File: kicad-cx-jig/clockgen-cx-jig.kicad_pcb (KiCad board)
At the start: 2 copper layers, 20.2 x 12 mm, 10 parts, among them J1 Conn_Coaxial, J2 Conn_01x01_Pin, J3 Conn_01x01_Pin, J4 Conn_01x01_Pin, J5 Conn_01x01_Pin

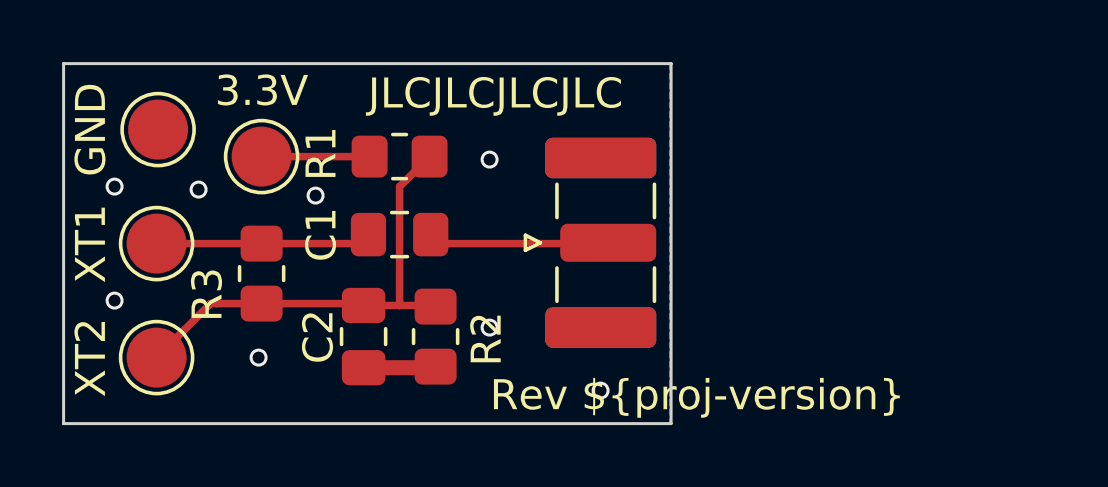
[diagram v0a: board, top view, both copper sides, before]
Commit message: Add board reference variable to project configuration
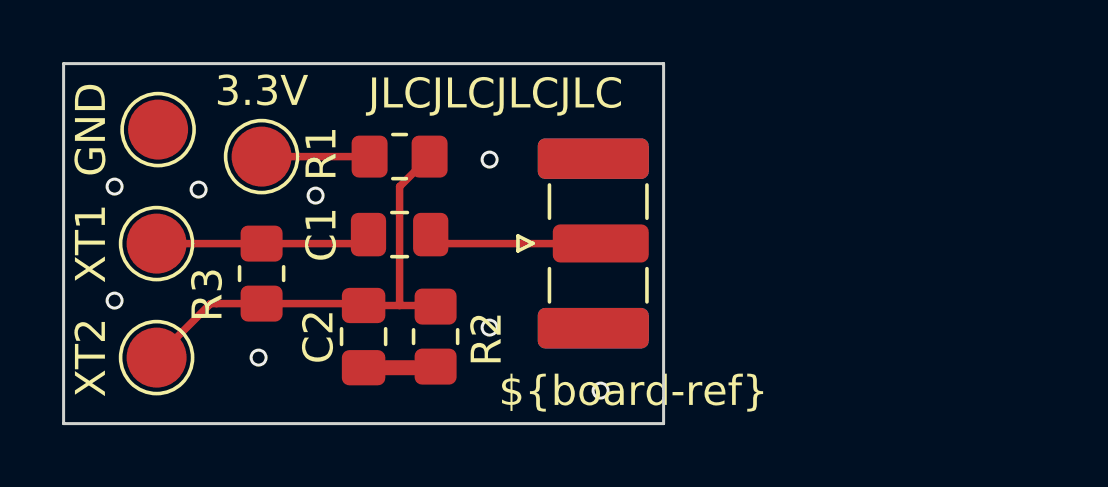
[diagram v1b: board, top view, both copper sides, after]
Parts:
- added ${board-ref}**: Board, PCM_kikit:Board, F.Cu at (125.0, 75.0)
- moved J1 0.25 mm to (142.9, 81.0)
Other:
- board size 20.2 x 12 mm -> 20 x 12 mm
- board text added: "${board-ref}"
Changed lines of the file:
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@@
 		(capping no)
 		(filling no)
-		(zone_defaults)
 		(pcbplotparams
 			(layerselection 0x00000000_00000000_55555555_5755f5ff)
@@
 		)
 	)
+	(property "board-ref" "CX_JIG")
 	(property "proj-author" "Reece Dodge")
 	(property "proj-company" "GDH Technologies LLC")
@@
 			(at 0 2.05 0)
 			(layer "F.Fab")
+			(hide yes)
 			(effects
 				(font
@@
 		(embedded_fonts no)
 	)
+	(footprint "PCM_kikit:Board"
+		(layer "F.Cu")
+		(at 125 75)
+		(descr "Mark board for extraction")
+		(property "Reference" "${board-ref}**"
+			(at -4.5 -5 0)
+			(layer "Dwgs.User")
+			(effects
+				(font
+					(size 1 1)
+					(thickness 0.15)
+				)
+				(justify left)
+			)
+		)
+		(property "Value" "Board"
+			(at -7.25 -5 0)
+			(layer "Dwgs.User")
+			(effects
+				(font
+					(size 1 1)
+					(thickness 0.15)
+				)
+			)
+		)
+		(property "Datasheet" ""
+			(at 0 0 0)
+			(layer "F.Fab")
+			(hide yes)
+			(effects
+				(font
+					(size 1.27 1.27)
+				)
+			)
+		)
+		(property "Description" ""
+			(at 0 0 0)
+			(layer "F.Fab")
+			(hide yes)
+			(effects
+				(font
+					(size 1.27 1.27)
+				)
+			)
+		)
+		(attr board_only exclude_from_pos_files exclude_from_bom allow_missing_courtyard)
+		(duplicate_pad_numbers_are_jumpers no)
+		(fp_line
+			(start -1.25 -4)
+			(end -9.25 -4)
+			(stroke
+				(width 0.2)
+				(type solid)
+			)
+			(layer "Dwgs.User")
+		)
+		(fp_line
+			(start 0 0)
+			(end -1.25 -4)
+			(stroke
+				(width 0.2)
+				(type solid)
+			)
+			(layer "Dwgs.User")
+		)
+		(fp_line
+			(start 0 0)
+			(end -1 -0.5)
+			(stroke
+				(width 0.2)
+				(type solid)
+			)
+			(layer "Dwgs.User")
+		)
+		(fp_line
+			(start 0 0)
+			(end 0.5 -1)
+			(stroke
+				(width 0.2)
+				(type solid)
+			)
+			(layer "Dwgs.User")
+		)
+		(embedded_fonts no)
+	)
 	(footprint "Resistor_SMD:R_0805_2012Metric_Pad1.20x1.40mm_HandSolder"
 		(layer "F.Cu")
@@
 	(footprint "Connector_Coaxial:SMA_Samtec_SMA-J-P-H-ST-EM1_EdgeMount"
 		(layer "F.Cu")
-		(at 143.155182 80.972275)
+		(at 142.905182 80.99455)
 		(descr "Connector SMA, 0Hz to 20GHz, 50Ohm, Edge Mount (http://suddendocs.samtec.com/prints/sma-j-p-x-st-em1-mkt.pdf)")
 		(tags "SMA Straight Samtec Edge Mount")
@@
 			(at 0 7.62 0)
 			(layer "F.Fab")
+			(hide yes)
 			(effects
 				(font
@@
 					(size 0.5 0.5)
 					(thickness 0.1)
-				)
-			)
-		)
-		(fp_text user "Board Thickness: 1.57mm"
-			(at 0 5.079999 0)
-			(layer "Cmts.User")
-			(effects
-				(font
-					(size 1 1)
-					(thickness 0.15)
 				)
 			)
@@
 			(at 0 2.05 0)
 			(layer "F.Fab")
+			(hide yes)
 			(effects
 				(font
@@
 			(layer "F.CrtYd")
 		)
-		(fp_text user "${REFERENCE}"
-			(at 0 -2 0)
-			(layer "F.Fab")
-			(effects
-				(font
-					(size 1 1)
-					(thickness 0.15)
-				)
-			)
-		)
 		(pad "1" smd circle
 			(at 0 0)
@@
 			(at 0 2.05 0)
 			(layer "F.Fab")
+			(hide yes)
 			(effects
 				(font
@@
 	(gr_rect
 		(start 125 75)
-		(end 145.25 87)
+		(end 145 87)
+		(radius 1)
 		(stroke
 			(width 0.1)
-			(type default)
+			(type solid)
 		)
 		(fill no)
 		(layer "Edge.Cuts")
 	)
-	(gr_text "Rev ${REVISION}"
-		(at 139.210441 86.641979 0)
+	(gr_text "${board-ref}"
+		(at 139.5 86.5 0)
 		(layer "F.SilkS")
 		(effects
@@
 			)
 			(justify bottom)
+		)
+	)
+	(gr_text "Rev ${REVISION}"
+		(at 144.710441 86.641979 -0)
+		(layer "B.SilkS")
+		(effects
+			(font
+				(size 1 1)
+				(thickness 0.15)
+			)
+			(justify left bottom mirror)
 		)
 	)
@@
 		)
 		(knockout no)
+	)
+	(point
+		(at 125 75)
+		(size 1)
+		(layer "Dwgs.User")
+	)
+	(point
+		(at 125 87)
+		(size 1)
+		(layer "Dwgs.User")
+	)
+	(point
+		(at 145 75)
+		(size 1)
+		(layer "Dwgs.User")
+	)
+	(point
+		(at 145 87)
+		(size 1)
+		(layer "Dwgs.User")
 	)
 	(segment
@@
 	(zone
 		(net "GND")
-		(layer "F.Cu")
+		(layers "F.Cu" "B.Cu")
+		(name "GND_PLANE")
 		(hatch edge 0.5)
 		(connect_pads
@@
 		(polygon
 			(pts
-				(xy 125 75) (xy 145.2 75) (xy 145.2 87) (xy 125 87)
-			)
-		)
-	)
-	(zone
-		(net "GND")
-		(layer "B.Cu")
-		(hatch edge 0.5)
-		(priority 1)
-		(connect_pads
-			(clearance 0.25)
-		)
-		(min_thickness 0.25)
-		(fill yes
-			(thermal_gap 0.5)
-			(thermal_bridge_width 0.5)
-			(island_removal_mode 0)
-		)
-		(polygon
-			(pts
-				(xy 125 75) (xy 145.2 75) (xy 145.2 87) (xy 125 87)
-			)
-		)
+				(xy 125 75) (xy 145 75) (xy 145 87) (xy 125 87)
+			)
+		)
